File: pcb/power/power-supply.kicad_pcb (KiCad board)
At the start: 2 copper layers, 42.5 x 21 mm, 10 parts, among them P1 CONN_01X03, P2 CONN_01X04, U1 7805, U2 78L06, U3 79L06

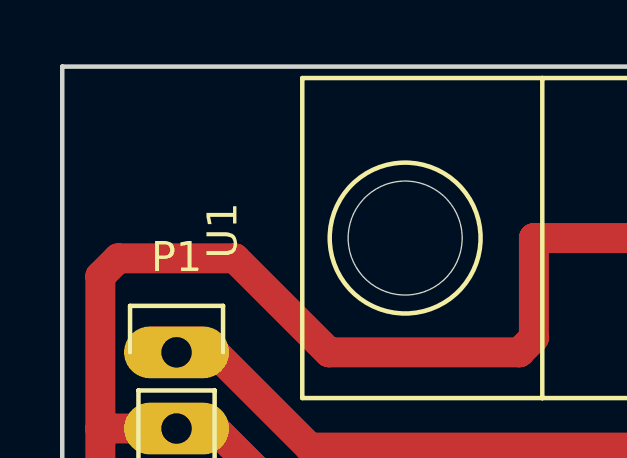
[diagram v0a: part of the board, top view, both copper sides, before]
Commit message: o Add marking.
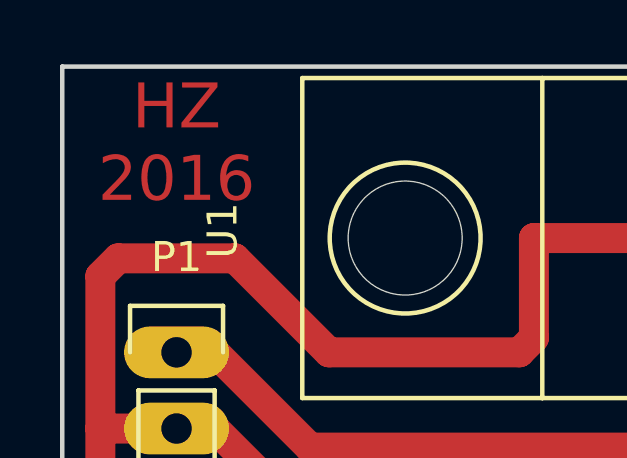
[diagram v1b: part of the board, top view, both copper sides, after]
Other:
- board text added: "HZ 2016"
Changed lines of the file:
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@@
     (links 24)
     (no_connects 0)
-    (area 116.764999 50.724999 158.190001 71.830001)
+    (area 115.1975 50.724999 171.195001 77.675001)
     (thickness 1.6)
-    (drawings 6)
+    (drawings 7)
     (tracks 78)
     (zones 0)
@@
     (fp_line (start 1 -1.025) (end -1 -1.025) (layer F.SilkS) (width 0.15))
     (fp_line (start -1 1.025) (end 1 1.025) (layer F.SilkS) (width 0.15))
-    (pad 2 smd rect (at 2 0 270) (size 2 1.6) (layers F.Cu F.Paste F.Mask)
-      (net 1 GND))
     (pad 1 smd rect (at -2 0 270) (size 2 1.6) (layers F.Cu F.Paste F.Mask)
       (net 5 /+15V))
+    (pad 2 smd rect (at 2 0 270) (size 2 1.6) (layers F.Cu F.Paste F.Mask)
+      (net 1 GND))
     (model Capacitors_SMD.3dshapes/C_1206_HandSoldering.wrl
       (at (xyz 0 0 0))
@@
     (fp_line (start -3.3 1.15) (end 3.3 1.15) (layer F.CrtYd) (width 0.05))
     (fp_line (start -3.3 -1.15) (end 3.3 -1.15) (layer F.CrtYd) (width 0.05))
+    (pad 2 smd rect (at 2 0 180) (size 2 1.6) (layers F.Cu F.Paste F.Mask)
+      (net 1 GND))
     (pad 1 smd rect (at -2 0 180) (size 2 1.6) (layers F.Cu F.Paste F.Mask)
       (net 6 /-15V))
-    (pad 2 smd rect (at 2 0 180) (size 2 1.6) (layers F.Cu F.Paste F.Mask)
-      (net 1 GND))
     (model Capacitors_SMD.3dshapes/C_1206_HandSoldering.wrl
       (at (xyz 0 0 0))
@@
     (fp_line (start 0.5 -0.85) (end -0.5 -0.85) (layer F.SilkS) (width 0.15))
     (fp_line (start -0.5 0.85) (end 0.5 0.85) (layer F.SilkS) (width 0.15))
-    (pad 2 smd rect (at 1.25 0 270) (size 1.5 1.25) (layers F.Cu F.Paste F.Mask)
-      (net 1 GND))
     (pad 1 smd rect (at -1.25 0 270) (size 1.5 1.25) (layers F.Cu F.Paste F.Mask)
       (net 2 /-6V))
+    (pad 2 smd rect (at 1.25 0 270) (size 1.5 1.25) (layers F.Cu F.Paste F.Mask)
+      (net 1 GND))
     (model Capacitors_SMD.3dshapes/C_0805_HandSoldering.wrl
       (at (xyz 0 0 0))
@@
     (fp_line (start 0.5 -0.85) (end -0.5 -0.85) (layer F.SilkS) (width 0.15))
     (fp_line (start -0.5 0.85) (end 0.5 0.85) (layer F.SilkS) (width 0.15))
-    (pad 2 smd rect (at 1.25 0 90) (size 1.5 1.25) (layers F.Cu F.Paste F.Mask)
-      (net 1 GND))
     (pad 1 smd rect (at -1.25 0 90) (size 1.5 1.25) (layers F.Cu F.Paste F.Mask)
       (net 3 /+5V))
+    (pad 2 smd rect (at 1.25 0 90) (size 1.5 1.25) (layers F.Cu F.Paste F.Mask)
+      (net 1 GND))
     (model Capacitors_SMD.3dshapes/C_0805_HandSoldering.wrl
       (at (xyz 0 0 0))
@@
     (fp_line (start -2.3 1) (end 2.3 1) (layer F.CrtYd) (width 0.05))
     (fp_line (start -2.3 -1) (end 2.3 -1) (layer F.CrtYd) (width 0.05))
+    (pad 2 smd rect (at 1.25 0 270) (size 1.5 1.25) (layers F.Cu F.Paste F.Mask)
+      (net 1 GND))
     (pad 1 smd rect (at -1.25 0 270) (size 1.5 1.25) (layers F.Cu F.Paste F.Mask)
       (net 4 /+6V))
-    (pad 2 smd rect (at 1.25 0 270) (size 1.5 1.25) (layers F.Cu F.Paste F.Mask)
-      (net 1 GND))
     (model Capacitors_SMD.3dshapes/C_0805_HandSoldering.wrl
       (at (xyz 0 0 0))
@@
     (fp_line (start -1.55 0) (end -1.55 -1.55) (layer F.SilkS) (width 0.15))
     (fp_line (start -1.55 -1.55) (end 1.55 -1.55) (layer F.SilkS) (width 0.15))
+    (pad 1 thru_hole oval (at 0 0) (size 3.5 1.7272) (drill 1.016) (layers *.Cu *.Mask F.SilkS)
+      (net 5 /+15V))
+    (pad 2 thru_hole oval (at 0 2.54) (size 3.5 1.7272) (drill 1.016) (layers *.Cu *.Mask F.SilkS)
+      (net 1 GND))
     (pad 3 thru_hole oval (at 0 5.08) (size 3.5 1.7272) (drill 1.016) (layers *.Cu *.Mask F.SilkS)
       (net 6 /-15V))
-    (pad 2 thru_hole oval (at 0 2.54) (size 3.5 1.7272) (drill 1.016) (layers *.Cu *.Mask F.SilkS)
-      (net 1 GND))
-    (pad 1 thru_hole oval (at 0 0) (size 3.5 1.7272) (drill 1.016) (layers *.Cu *.Mask F.SilkS)
-      (net 5 /+15V))
     (model Pin_Headers.3dshapes/Pin_Header_Straight_1x03.wrl
       (at (xyz 0 -0.1 0))
@@
     (fp_line (start -1.55 0) (end -1.55 -1.55) (layer F.SilkS) (width 0.15))
     (fp_line (start -1.55 -1.55) (end 1.55 -1.55) (layer F.SilkS) (width 0.15))
+    (pad 1 thru_hole rect (at 0 0) (size 3.5 1.7272) (drill 1.016) (layers *.Cu *.Mask F.SilkS)
+      (net 3 /+5V))
+    (pad 2 thru_hole oval (at 0 2.54) (size 3.5 1.7272) (drill 1.016) (layers *.Cu *.Mask F.SilkS)
+      (net 4 /+6V))
+    (pad 3 thru_hole oval (at 0 5.08) (size 3.5 1.7272) (drill 1.016) (layers *.Cu *.Mask F.SilkS)
+      (net 1 GND))
     (pad 4 thru_hole oval (at 0 7.62) (size 3.5 1.7272) (drill 1.016) (layers *.Cu *.Mask F.SilkS)
       (net 2 /-6V))
-    (pad 3 thru_hole oval (at 0 5.08) (size 3.5 1.7272) (drill 1.016) (layers *.Cu *.Mask F.SilkS)
-      (net 1 GND))
-    (pad 2 thru_hole oval (at 0 2.54) (size 3.5 1.7272) (drill 1.016) (layers *.Cu *.Mask F.SilkS)
-      (net 4 /+6V))
-    (pad 1 thru_hole rect (at 0 0) (size 3.5 1.7272) (drill 1.016) (layers *.Cu *.Mask F.SilkS)
-      (net 3 /+5V))
     (model Pin_Headers.3dshapes/Pin_Header_Straight_1x04.wrl
       (at (xyz 0 -0.15 0))
@@
       (effects (font (size 1 1) (thickness 0.15)))
     )
-    (fp_text value 79L06 (at 6.35 1.27 360) (layer F.Fab)
+    (fp_text value 79L06 (at 6.35 1.27) (layer F.Fab)
       (effects (font (size 1 1) (thickness 0.15)))
     )
@@
     (fp_line (start 2.25044 -1.30048) (end 2.25044 0.50038) (layer F.SilkS) (width 0.15))
     (fp_line (start 2.25044 -1.30048) (end 1.6002 -1.30048) (layer F.SilkS) (width 0.15))
-    (pad 2 smd trapezoid (at 0 0.7493 90) (size 1.50114 0.7493) (rect_delta 0 0.50038 ) (layers F.Cu F.Paste F.Mask)
-      (net 6 /-15V))
-    (pad 2 smd rect (at 0 -1.6002 270) (size 1.99898 4.0005) (layers F.Cu F.Paste F.Mask)
+    (pad 1 smd rect (at -1.50114 2.35204 270) (size 1.00076 2.5019) (layers F.Cu F.Paste F.Mask)
+      (net 1 GND))
+    (pad 2 smd rect (at 0 2.35204 270) (size 1.00076 2.5019) (layers F.Cu F.Paste F.Mask)
       (net 6 /-15V))
     (pad 3 smd rect (at 1.50114 2.35204 270) (size 1.00076 2.5019) (layers F.Cu F.Paste F.Mask)
       (net 2 /-6V))
-    (pad 2 smd rect (at 0 2.35204 270) (size 1.00076 2.5019) (layers F.Cu F.Paste F.Mask)
+    (pad 2 smd rect (at 0 -1.6002 270) (size 1.99898 4.0005) (layers F.Cu F.Paste F.Mask)
       (net 6 /-15V))
-    (pad 1 smd rect (at -1.50114 2.35204 270) (size 1.00076 2.5019) (layers F.Cu F.Paste F.Mask)
-      (net 1 GND))
+    (pad 2 smd trapezoid (at 0 0.7493 90) (size 1.50114 0.7493) (rect_delta 0 0.50038 ) (layers F.Cu F.Paste F.Mask)
+      (net 6 /-15V))
     (model TO_SOT_Packages_SMD.3dshapes/SOT89-3_Housing_Handsoldering.wrl
       (at (xyz 0 0 0))
@@
     (fp_line (start 0 -3.683) (end -5.334 -3.683) (layer F.SilkS) (width 0.15))
     (fp_line (start 0 -3.683) (end 5.334 -3.683) (layer F.SilkS) (width 0.15))
-    (pad "" np_thru_hole circle (at 0 -16.764 180) (size 3.79984 3.79984) (drill 3.79984) (layers *.Cu *.Mask F.SilkS))
+    (pad 2 thru_hole oval (at 0 0 180) (size 3.50012 1.69926) (drill 1.00076) (layers *.Cu *.Mask F.SilkS)
+      (net 1 GND))
+    (pad 1 thru_hole oval (at -2.54 0 180) (size 3.50012 1.69926) (drill 1.00076) (layers *.Cu *.Mask F.SilkS)
+      (net 5 /+15V))
     (pad 3 thru_hole oval (at 2.54 0 180) (size 3.50012 1.69926) (drill 1.00076) (layers *.Cu *.Mask F.SilkS)
       (net 3 /+5V))
-    (pad 1 thru_hole oval (at -2.54 0 180) (size 3.50012 1.69926) (drill 1.00076) (layers *.Cu *.Mask F.SilkS)
-      (net 5 /+15V))
-    (pad 2 thru_hole oval (at 0 0 180) (size 3.50012 1.69926) (drill 1.00076) (layers *.Cu *.Mask F.SilkS)
-      (net 1 GND))
+    (pad "" np_thru_hole circle (at 0 -16.764 180) (size 3.79984 3.79984) (drill 3.79984) (layers *.Cu *.Mask F.SilkS))
     (model TO_SOT_Packages_THT.3dshapes/TO-220_Neutral123_Horizontal_LargePads.wrl
       (at (xyz 0 0 0))
@@
     (fp_line (start 2.25044 -1.30048) (end 2.25044 0.50038) (layer F.SilkS) (width 0.15))
     (fp_line (start 2.25044 -1.30048) (end 1.6002 -1.30048) (layer F.SilkS) (width 0.15))
-    (pad 2 smd trapezoid (at 0 0.7493) (size 1.50114 0.7493) (rect_delta 0 0.50038 ) (layers F.Cu F.Paste F.Mask)
-      (net 1 GND))
-    (pad 2 smd rect (at 0 -1.6002 180) (size 1.99898 4.0005) (layers F.Cu F.Paste F.Mask)
+    (pad 1 smd rect (at -1.50114 2.35204 180) (size 1.00076 2.5019) (layers F.Cu F.Paste F.Mask)
+      (net 4 /+6V))
+    (pad 2 smd rect (at 0 2.35204 180) (size 1.00076 2.5019) (layers F.Cu F.Paste F.Mask)
       (net 1 GND))
     (pad 3 smd rect (at 1.50114 2.35204 180) (size 1.00076 2.5019) (layers F.Cu F.Paste F.Mask)
       (net 5 /+15V))
-    (pad 2 smd rect (at 0 2.35204 180) (size 1.00076 2.5019) (layers F.Cu F.Paste F.Mask)
-      (net 1 GND))
-    (pad 1 smd rect (at -1.50114 2.35204 180) (size 1.00076 2.5019) (layers F.Cu F.Paste F.Mask)
-      (net 4 /+6V))
+    (pad 2 smd rect (at 0 -1.6002 180) (size 1.99898 4.0005) (layers F.Cu F.Paste F.Mask)
+      (net 1 GND))
+    (pad 2 smd trapezoid (at 0 0.7493) (size 1.50114 0.7493) (rect_delta 0 0.50038 ) (layers F.Cu F.Paste F.Mask)
+      (net 1 GND))
     (model TO_SOT_Packages_SMD.3dshapes/SOT89-3_Housing_Handsoldering.wrl
       (at (xyz 0 0 0))
@@
     )
   )
+  (gr_text "HZ\n2016" (at 120.65 53.34) (layer F.Cu)
+    (effects (font (size 1.5 1.5) (thickness 0.3)))
+  )
   (dimension 42.545 (width 0.3) (layer Dwgs.User)

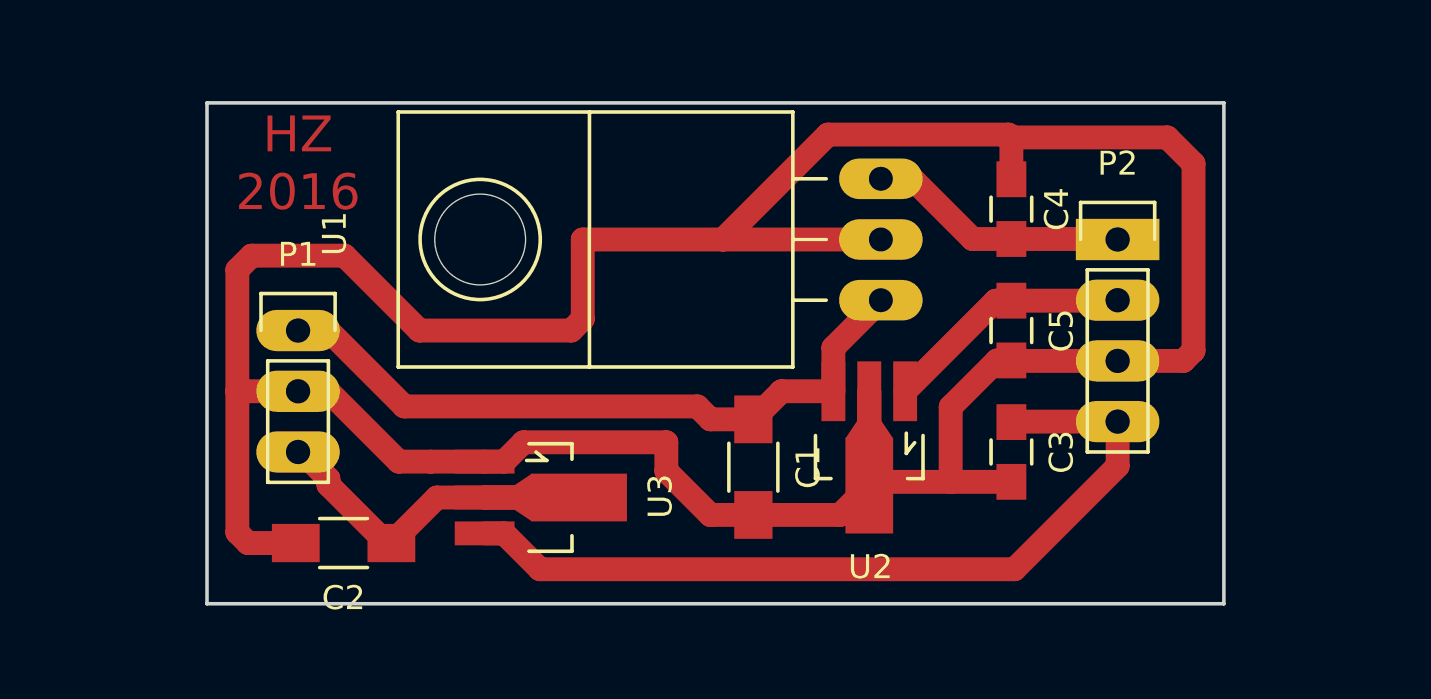
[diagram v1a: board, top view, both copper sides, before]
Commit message: o Add pull-ups for I2C bus. o smallish changes in power supply.
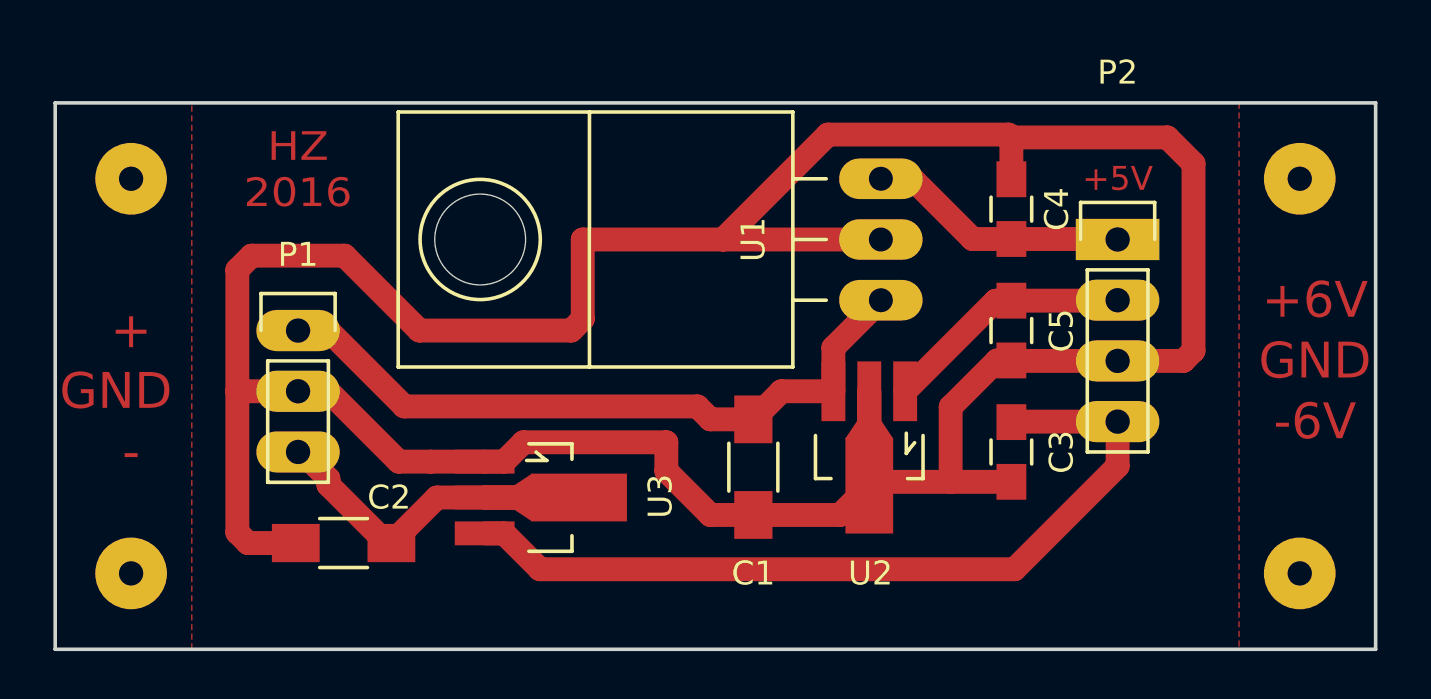
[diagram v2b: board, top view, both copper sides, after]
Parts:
- added R: D, Pin_Headers:Pin_Header_Straight_1x01, F.Cu at (162.6, 70.5)
- added R: D, Pin_Headers:Pin_Header_Straight_1x01, F.Cu at (162.6, 54.0)
- added R: D, Pin_Headers:Pin_Header_Straight_1x01, F.Cu at (113.7, 70.5)
- added R: D, Pin_Headers:Pin_Header_Straight_1x01, F.Cu at (113.7, 54.0)
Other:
- board size 42.5 x 21 mm -> 55.2 x 22.9 mm
- board text added: "+"
- board text added: "+5V"
- board text added: "+6V"
- board text added: "-"
- board text added: "-6V"
- board text added: "GND"
